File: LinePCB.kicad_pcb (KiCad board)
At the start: 4 copper layers, 178 x 169.8 mm, 222 parts, among them J1 Conn_01x12, J3 Conn_01x03, U1 MCP3008, U10 Optocoupler, U11 210, U12 2200, U13 2200, U14 210, U15 Oprocoupler, U16 10k, U17 N channel, U18 D, U19 10K, U2 MCP3008, U20 Conn_01x02, U3 MCP3008, U4 MCP3008, U5 MCP3008, U6 MCP3008, U7 30k, U8 115k, U9 BSP89

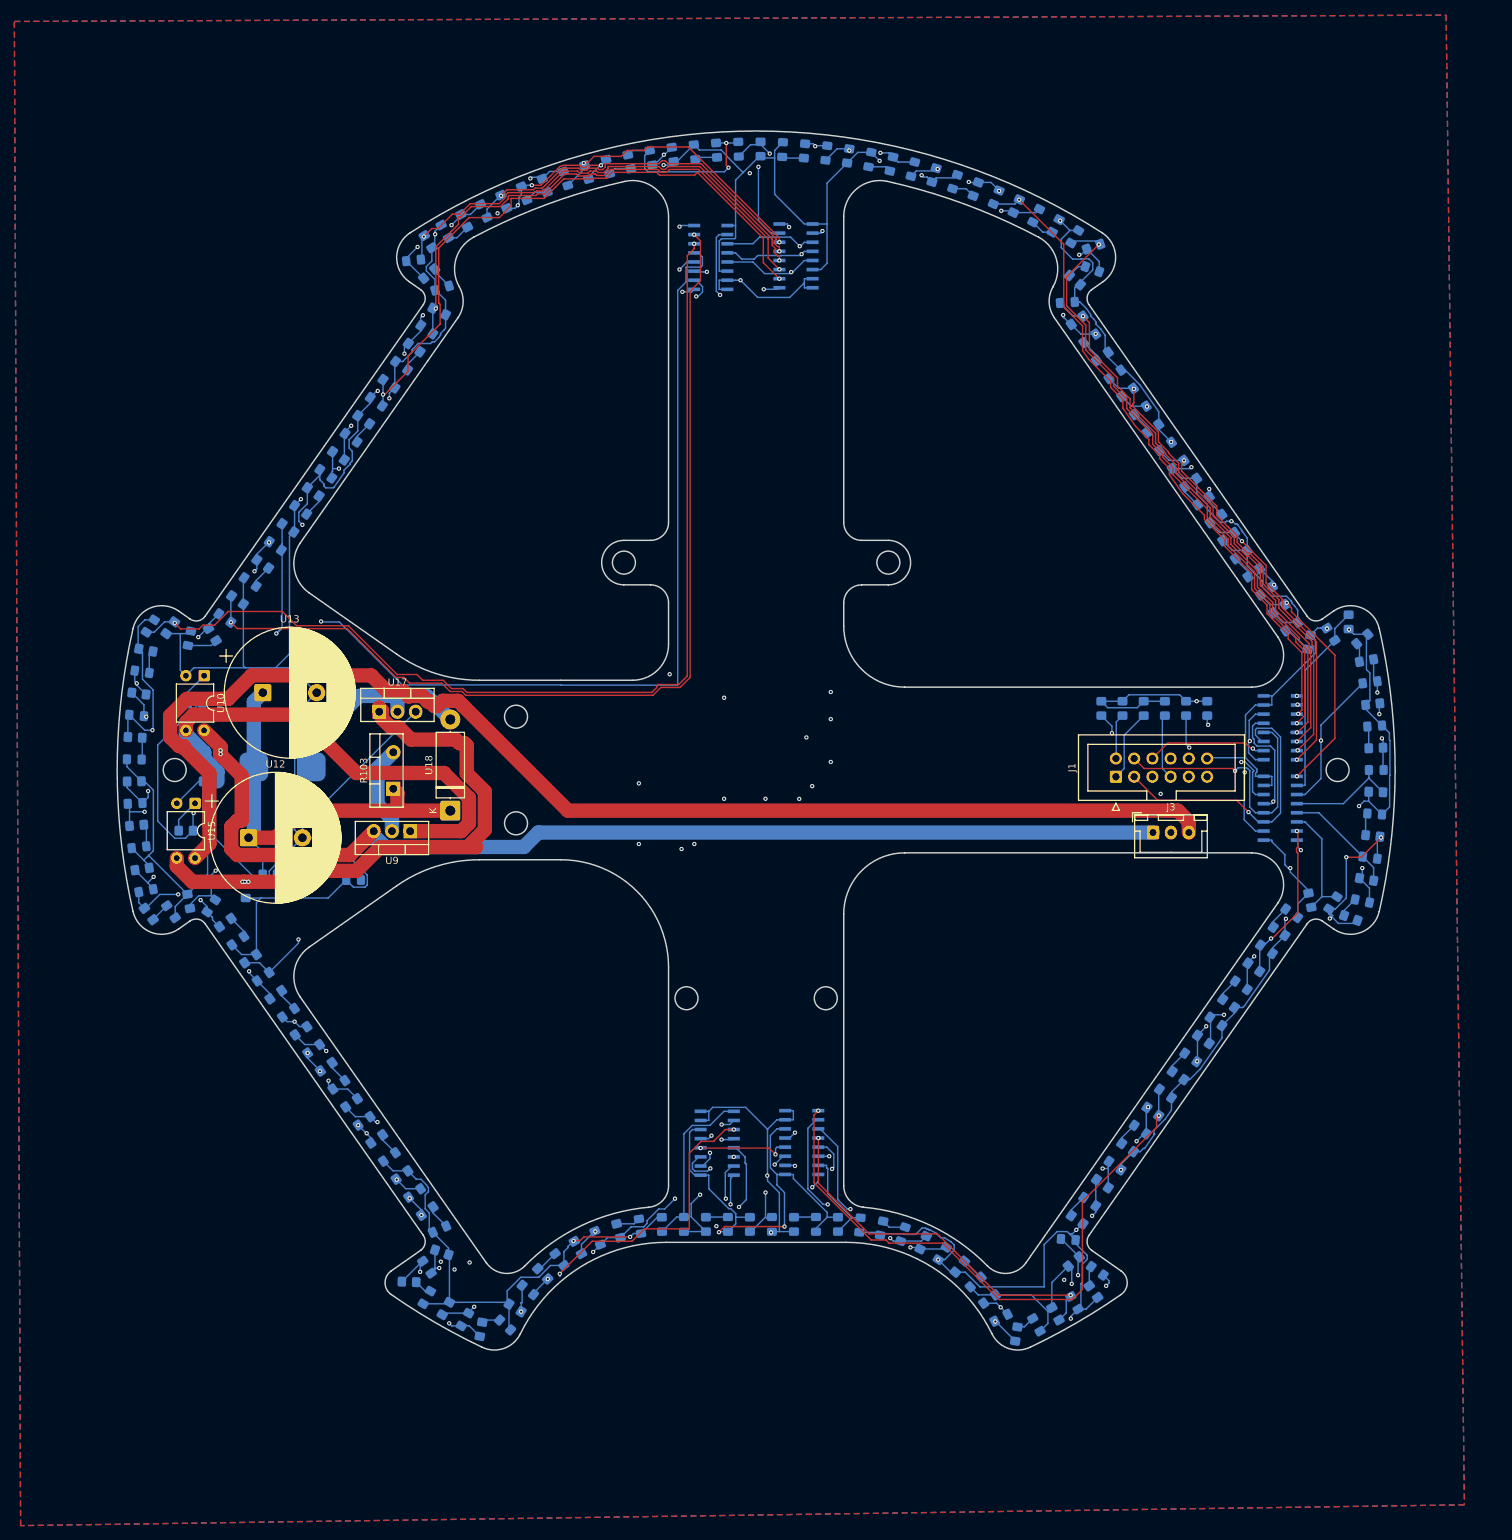
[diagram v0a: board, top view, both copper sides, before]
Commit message: added voltage reg
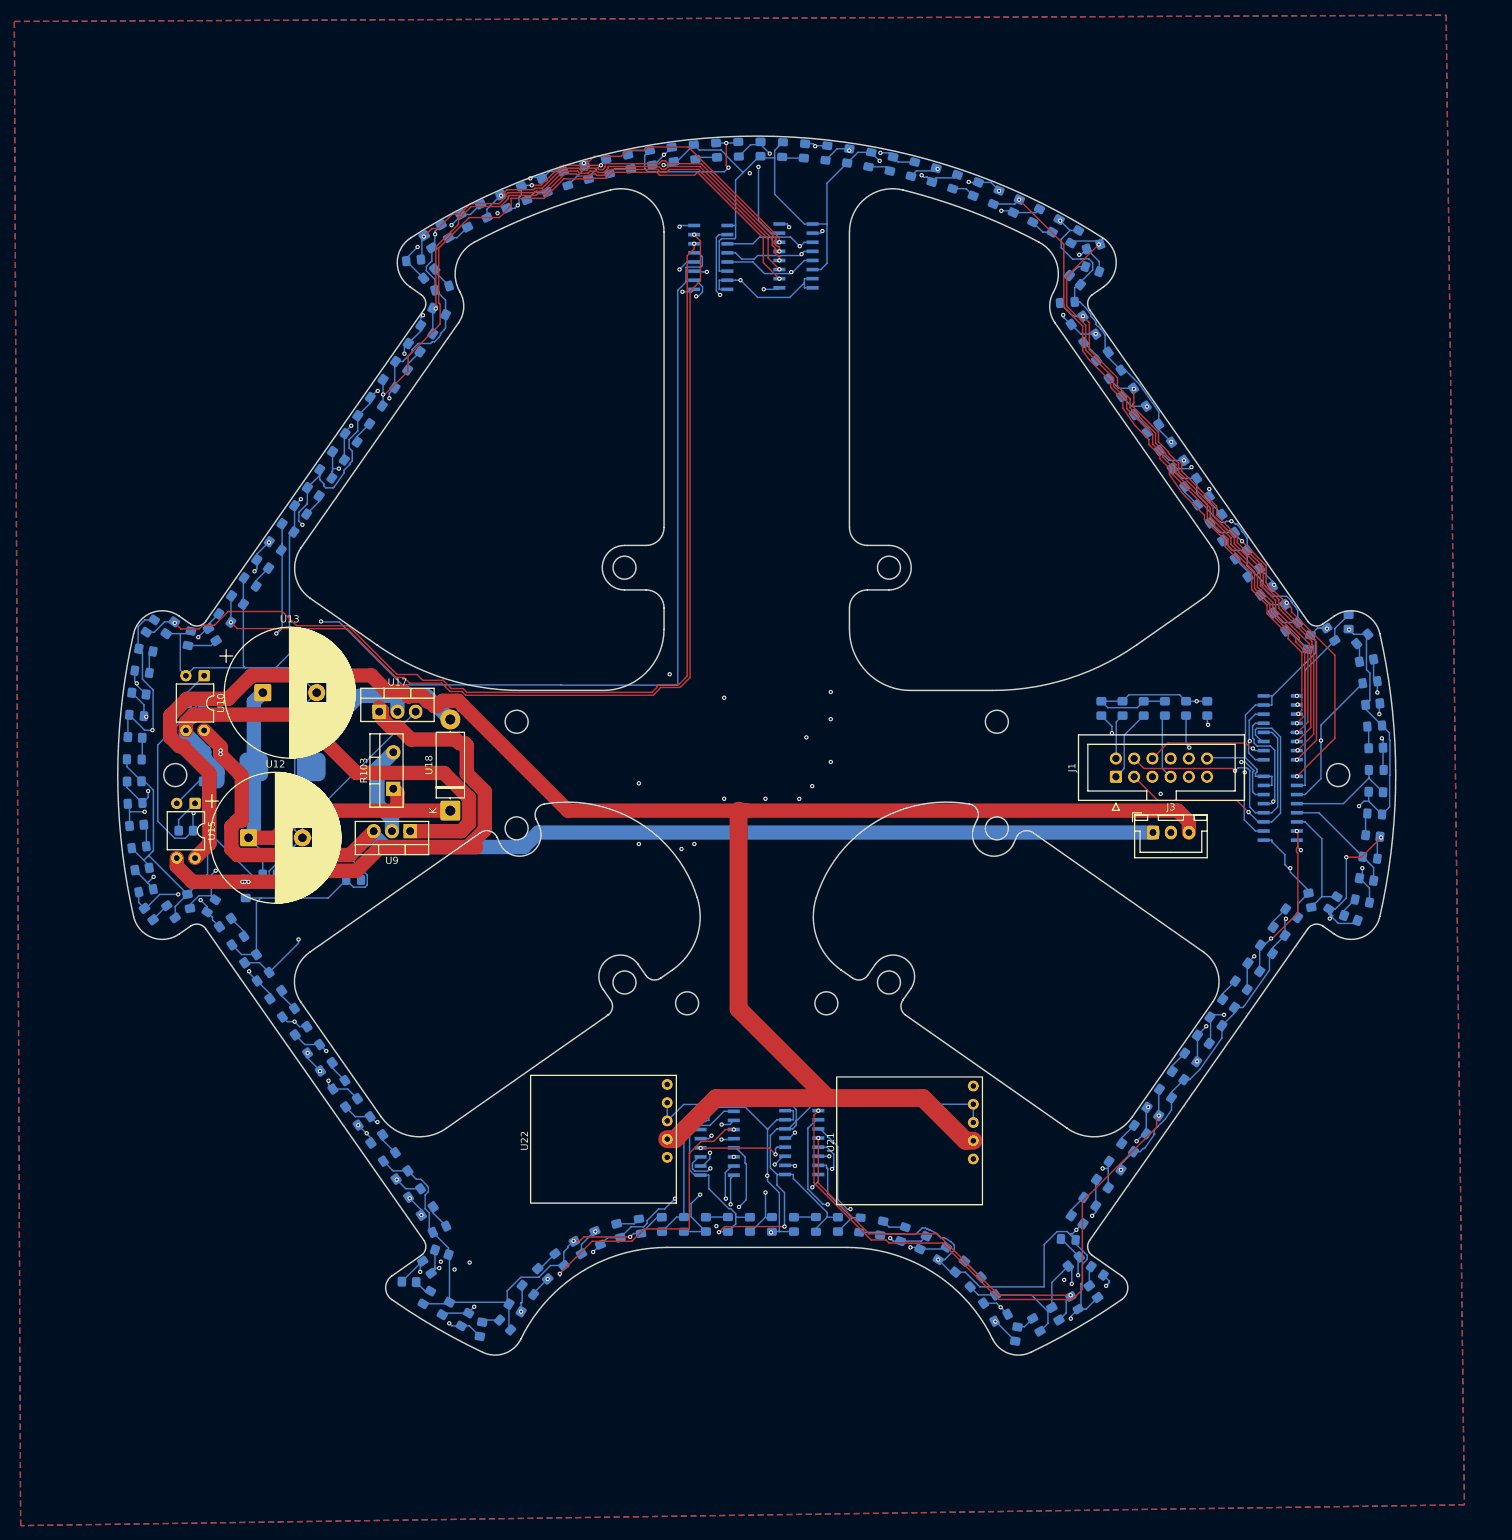
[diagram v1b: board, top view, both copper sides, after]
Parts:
- added U21: V_Regulator3.3v, Custom1:Pololu5V3.4A, F.Cu at (131.5, 160.6)
- added U22: V_Regulator5v, Custom1:Pololu5V3.4A, F.Cu at (88.9, 160.3)
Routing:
- net 12V: track 178.1 -> 272.1 mm
- net GND: track 1082.6 -> 1138.4 mm
- net 3.3V: track 966.5 -> 992.6 mm
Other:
- outline, holes or cut-outs redrawn

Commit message: rotated everything
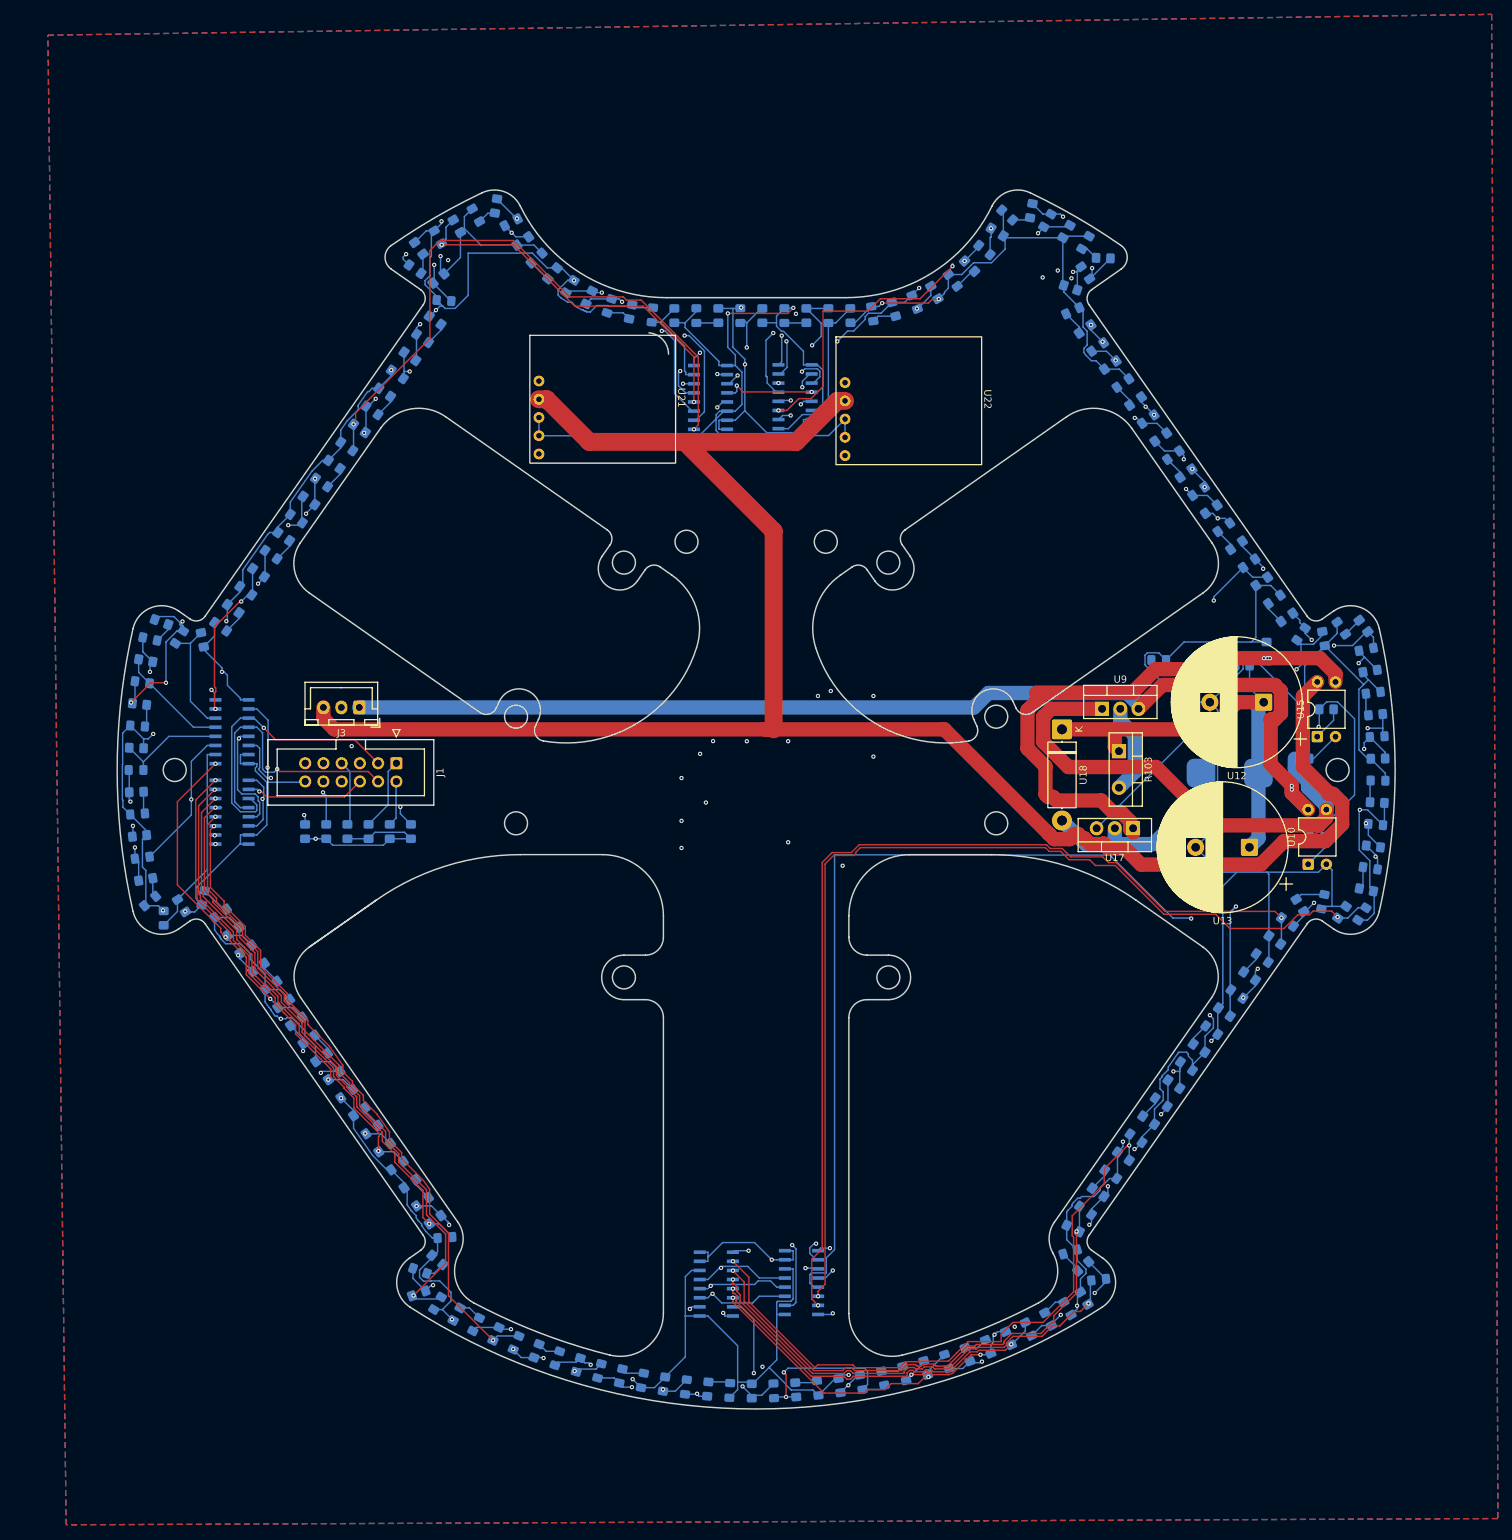
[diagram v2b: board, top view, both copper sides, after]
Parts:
- moved R67 173.9 mm to (184.6, 79.9), turned to 127 degrees
- moved R44 173.6 mm to (138.3, 22.1), turned to -100 degrees
- moved D67 173.5 mm to (184.4, 120.0), turned to -123 degrees
- moved R20 173.5 mm to (53.0, 172.9), turned to 20 degrees
- moved D93 173.3 mm to (143.4, 175.0), turned to 120 degrees
- moved R77 173.3 mm to (140.7, 176.5), turned to 118 degrees
- moved R90 173.3 mm to (186.6, 98.4), turned to -179 degrees
- moved D85 173.3 mm to (186.6, 101.5), turned to 179 degrees
- moved D74 173.3 mm to (186.5, 95.3), turned to 3 degrees
- moved R69 173.3 mm to (186.5, 104.5), turned to 177 degrees
- moved D42 173.3 mm to (140.6, 23.5), turned to 60 degrees
- moved D70 173.3 mm to (186.3, 107.6), turned to -5 degrees
- moved R68 173.3 mm to (186.3, 92.3), turned to -175 degrees
- moved R86 173.3 mm to (186.0, 110.6), turned to 173 degrees
- moved D84 173.3 mm to (186.0, 89.2), turned to -173 degrees
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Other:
- outline, holes or cut-outs redrawn

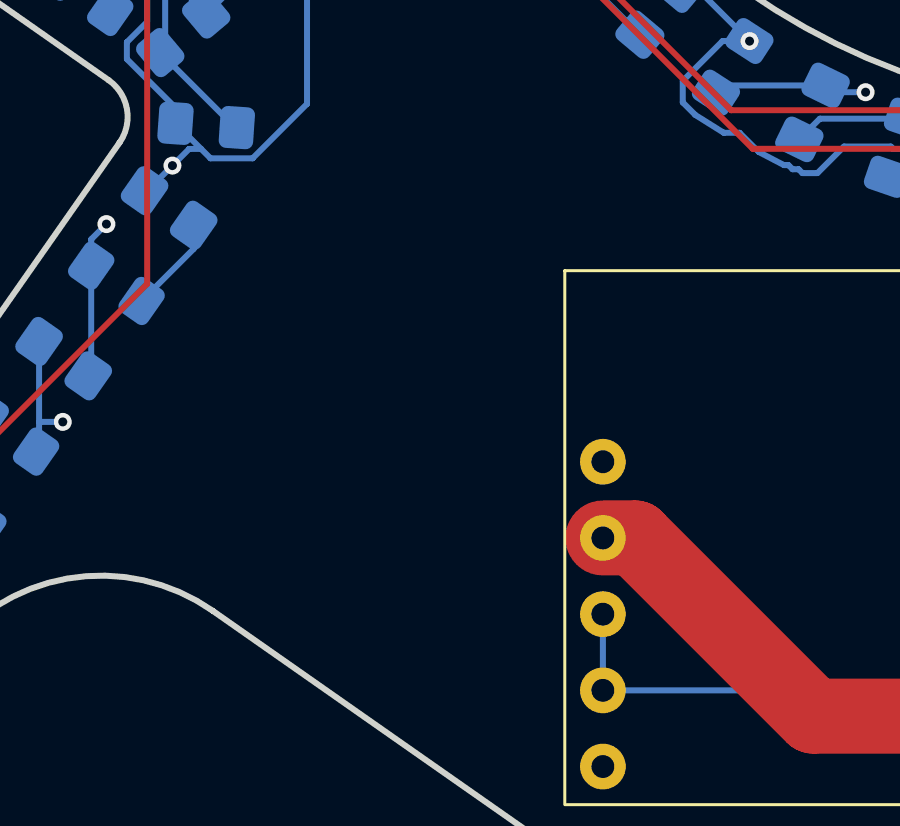
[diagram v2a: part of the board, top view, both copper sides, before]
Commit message: Added JST
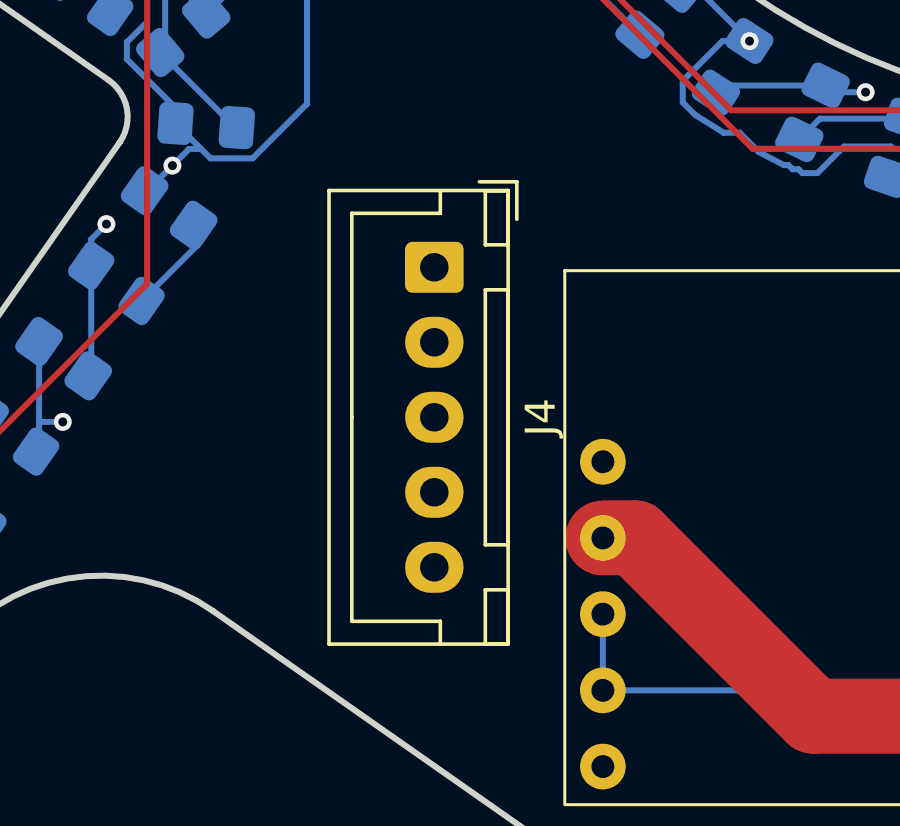
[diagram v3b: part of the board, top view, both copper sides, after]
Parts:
- added J4: Conn_01x05_Pin, Connector_JST:JST_XH_B5B-XH-A_1x05_P2.50mm_Vertical, F.Cu at (64.1, 39.3)

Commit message: mb didnt save some
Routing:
- net 48V: track 152.2 -> 312.7 mm, vias 2 -> 5
- net Kicker: track 170.1 -> 267.7 mm
- net 12V: track 272.1 -> 345.8 mm, vias 0 -> 4
- net 5V: track 0.00 -> 54.2 mm
- net 3.3V: track 992.6 -> 1010.7 mm, vias 53 -> 56
- net Ch33: track 150.8 -> 138.9 mm, vias 4 -> 2
- net SCK1: track 241.8 -> 251.5 mm
- net Net-(U9-G): track 66.9 -> 57.6 mm, vias 0 -> 2
- net GND: track 1138.4 -> 1145.7 mm
- net Net-(U17-G): track 77.8 -> 70.9 mm, vias 3 -> 2
- net Ch37: track 151.0 -> 145.3 mm, vias 2 -> 4
- net Ch34: track 156.2 -> 158.7 mm, vias 3 -> 2
- net CS4: track 126.1 -> 127.7 mm, vias 2 -> 1
- net Ch35: track 164.7 -> 165.0 mm, vias 3 -> 4
